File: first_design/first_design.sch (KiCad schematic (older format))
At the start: 56 parts, among them J1 Conn_02x20_Odd_Even, J2 Accelerometer_small, J3 Accelerometer_standard, J4 Servo_motor

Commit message: tracing
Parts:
- removed C7: 44uF, library_express_pro:RLC_EIA_3216, symbol Device:C
- removed D1: 5V, symbol Device:D_Zener
- removed R3: 100K, library_express_pro:RLC_EIA_3216, symbol Device:R
- C2: value 170uF -> 10uF
- SQJA37EP1: footprint (none) -> library_express_pro:SO-8L
- YSL-R531R3D-D1, YSL-R531R3D-D2, YSL-R531R3D-D3, YSL-R531R3D-D4: footprint library_express_pro:LED_YSL-R531R3D-D2 -> library_express_pro:RLC_EIA_3216
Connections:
- wire segments 154 -> 149
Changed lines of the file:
@@
-$EndComp
-$Comp
-L Device:D_Zener D1
-U 1 1 5D2FFD20
-P 1000 1200
-F 0 "D1" V 1046 1121 50  0000 R CNN
-F 1 "5V" V 955 1121 50  0000 R CNN
-F 2 "" H 1000 1200 50  0001 C CNN
-F 3 "~" H 1000 1200 50  0001 C CNN
-	1    1000 1200
-	0    -1   -1   0
 $EndComp
 $Comp
@@
 $EndComp
 Wire Wire Line
-	1000 1000 1500 1000
-Wire Wire Line
-	1000 1050 1000 1000
-Connection ~ 1000 1000
-Wire Wire Line
-	650  1000 1000 1000
-Wire Wire Line
 	1800 1400 1800 1350
 Wire Wire Line
-	1200 1350 1000 1350
-Wire Wire Line
 	1200 1400 1200 1350
-Connection ~ 1200 1350
 Connection ~ 1800 1350
 Wire Wire Line
@@
 P 1200 1550
 F 0 "C2" H 1082 1504 50  0001 R CNN
-F 1 "170uF" H 1082 1550 50  0000 R CNN
+F 1 "10uF" H 1082 1550 50  0000 R CNN
 F 2 "library_express_pro:RLC_EIA_3216" H 1238 1400 50  0001 C CNN
 F 3 "~" H 1200 1550 50  0001 C CNN
@@
 	1    0    0    -1
 $EndComp
-$Comp
-L Device:R R3
-U 1 1 5D63B556
-P 4400 1400
-F 0 "R3" V 4607 1400 50  0000 C CNN
-F 1 "100K" V 4516 1400 50  0000 C CNN
-F 2 "library_express_pro:RLC_EIA_3216" V 4330 1400 50  0001 C CNN
-F 3 "~" H 4400 1400 50  0001 C CNN
-	1    4400 1400
-	-1   0    0    1
-$EndComp
 Text GLabel 4250 1150 0    50   Input ~ 0
 Vbat
@@
 $EndComp
 $Comp
-L Device:C C9
-U 1 1 5D69FBE8
-P 6800 1700
-F 0 "C9" H 6685 1654 50  0000 R CNN
-F 1 "44uF" H 6685 1745 50  0000 R CNN
-F 2 "library_express_pro:RLC_EIA_3216" H 6838 1550 50  0001 C CNN
-F 3 "~" H 6800 1700 50  0001 C CNN
-	1    6800 1700
-	-1   0    0    1
-$EndComp
-$Comp
 L power:GND #PWR0111
 U 1 1 5D6AF0A6
@@
 F 0 "YSL-R531R3D-D2" H 5893 5445 50  0000 C CNN
 F 1 "LED" H 5893 5536 50  0000 C CNN
-F 2 "library_express_pro:LED_YSL-R531R3D-D2" H 5900 5700 50  0001 C CNN
+F 2 "library_express_pro:RLC_EIA_3216" H 5900 5700 50  0001 C CNN
 F 3 "~" H 5900 5700 50  0001 C CNN
 	1    5900 5700
@@
 F 0 "YSL-R531R3D-D1" H 5893 5995 50  0000 C CNN
 F 1 "LED" H 5893 6086 50  0000 C CNN
-F 2 "library_express_pro:LED_YSL-R531R3D-D2" H 5900 6250 50  0001 C CNN
+F 2 "library_express_pro:RLC_EIA_3216" H 5900 6250 50  0001 C CNN
 F 3 "~" H 5900 6250 50  0001 C CNN
 	1    5900 6250
@@
 F 0 "YSL-R531R3D-D3" H 5893 6545 50  0000 C CNN
 F 1 "LED" H 5893 6636 50  0000 C CNN
-F 2 "library_express_pro:LED_YSL-R531R3D-D2" H 5900 6800 50  0001 C CNN
+F 2 "library_express_pro:RLC_EIA_3216" H 5900 6800 50  0001 C CNN
 F 3 "~" H 5900 6800 50  0001 C CNN
 	1    5900 6800
@@
 F 0 "YSL-R531R3D-D4" H 5893 7045 50  0000 C CNN
 F 1 "LED" H 5893 7136 50  0000 C CNN
-F 2 "library_express_pro:LED_YSL-R531R3D-D2" H 5900 7300 50  0001 C CNN
+F 2 "library_express_pro:RLC_EIA_3216" H 5900 7300 50  0001 C CNN
 F 3 "~" H 5900 7300 50  0001 C CNN
 	1    5900 7300
@@
 	4600 1550 4400 1550
 Wire Wire Line
-	4400 1250 4400 1150
-Connection ~ 6800 1550
-Wire Wire Line
-	6800 1550 7000 1550
-Wire Wire Line
-	4600 1150 4400 1150
-Wire Wire Line
-	4250 1150 4400 1150
-Connection ~ 4400 1150
-Wire Wire Line
 	5350 1550 5450 1550
 Wire Wire Line
@@
 Wire Wire Line
 	6100 2300 6100 2650
-$Comp
-L Device:C C7
-U 1 1 5DB9C798
-P 6350 1800
-F 0 "C7" H 6235 1754 50  0000 R CNN
-F 1 "44uF" H 6235 1845 50  0000 R CNN
-F 2 "library_express_pro:RLC_EIA_3216" H 6388 1650 50  0001 C CNN
-F 3 "~" H 6350 1800 50  0001 C CNN
-	1    6350 1800
-	-1   0    0    1
-$EndComp
-Wire Wire Line
-	6350 1650 6100 1650
-Connection ~ 6100 1650
-Wire Wire Line
-	6350 1950 6100 1950
-Wire Wire Line
-	6100 1550 6800 1550
 Connection ~ 6100 1550
 Wire Wire Line
@@
 L Connector_Generic:Conn_01x03 J4
 U 1 1 5DD35231
-P 9800 6050
-F 0 "J4" H 9880 6092 50  0001 L CNN
-F 1 "Servo_motor" H 9880 6046 50  0000 L CNN
-F 2 "library_express_pro:servo_connector" H 9800 6050 50  0001 C CNN
-F 3 "~" H 9800 6050 50  0001 C CNN
-	1    9800 6050
-	1    0    0    -1
-$EndComp
-Text GLabel 9600 5950 0    50   Input ~ 0
+P 9800 6000
+F 0 "J4" H 9880 6042 50  0001 L CNN
+F 1 "Servo_motor" H 9880 5996 50  0000 L CNN
+F 2 "library_express_pro:servo_connector" H 9800 6000 50  0001 C CNN
+F 3 "~" H 9800 6000 50  0001 C CNN
+	1    9800 6000
+	1    0    0    -1
+$EndComp
+Text GLabel 9600 6000 0    50   Input ~ 0
 6V-5V
 $Comp
 L power:GND #PWR0126
 U 1 1 5DD3FB35
-P 9100 6050
-F 0 "#PWR0126" H 9100 5800 50  0001 C CNN
-F 1 "GND" V 9105 5922 50  0000 R CNN
-F 2 "" H 9100 6050 50  0001 C CNN
-F 3 "" H 9100 6050 50  0001 C CNN
-	1    9100 6050
+P 9100 5900
+F 0 "#PWR0126" H 9100 5650 50  0001 C CNN
+F 1 "GND" V 9105 5772 50  0000 R CNN
+F 2 "" H 9100 5900 50  0001 C CNN
+F 3 "" H 9100 5900 50  0001 C CNN
+	1    9100 5900
 	0    1    1    0
 $EndComp
-Text GLabel 9600 6150 0    50   Input ~ 0
+Text GLabel 9600 6100 0    50   Input ~ 0
 servo_PWM
 Wire Wire Line
-	9100 6050 9600 6050
+	9100 5900 9600 5900
 Text GLabel 10000 2900 2    50   Input ~ 0
 servo_PWM
@@
 F 0 "SQJA37EP1" H 1906 1046 50  0000 L CNN
 F 1 "PMOS" H 1906 1000 50  0000 L CNN
-F 2 "" H 1900 1100 50  0001 C CNN
+F 2 "library_express_pro:SO-8L" H 1900 1100 50  0001 C CNN
 F 3 "~" H 1700 1000 50  0001 C CNN
 	1    1700 1000
@@
 	1    0    0    -1
 $EndComp
+Wire Wire Line
+	6100 1550 6800 1550
+Wire Wire Line
+	6800 1550 7000 1550
+Connection ~ 6800 1550
+$Comp
+L Device:C C9
+U 1 1 5D69FBE8
+P 6800 1700
+F 0 "C9" H 6685 1654 50  0000 R CNN
+F 1 "44uF" H 6685 1745 50  0000 R CNN
+F 2 "library_express_pro:RLC_EIA_3216" H 6838 1550 50  0001 C CNN
+F 3 "~" H 6800 1700 50  0001 C CNN
+	1    6800 1700
+	-1   0    0    1
+$EndComp
+Connection ~ 4400 1150
+Wire Wire Line
+	4600 1150 4400 1150
+Wire Wire Line
+	4250 1150 4400 1150
+Wire Wire Line
+	4400 1150 4400 1550
+Wire Wire Line
+	650  1000 1500 1000
 $EndSCHEMATC

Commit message: traced buck
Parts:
- C9: footprint library_express_pro:RLC_EIA_3216 -> library_express_pro:Capacitor_E61
- J1: footprint library_express_pro:RasPi_header_pro -> library_express_pro:RasPi_Header_0.9
- L1: footprint library_express_pro:RLC_EIA_3216 -> library_express_pro:Inductor_PA4340
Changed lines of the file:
@@
 F 0 "J1" V 9654 2013 50  0001 R CNN
 F 1 "Conn_02x20_Odd_Even" H 9745 2013 50  0000 R CNN
-F 2 "library_express_pro:RasPi_header_pro" H 9650 3100 50  0001 C CNN
+F 2 "library_express_pro:RasPi_Header_0.9" H 9650 3100 50  0001 C CNN
 F 3 "~" H 9650 3100 50  0001 C CNN
 	1    9650 3100
@@
 F 0 "L1" V 5519 1550 50  0000 C CNN
 F 1 "3.3uH" V 5610 1550 50  0000 C CNN
-F 2 "library_express_pro:RLC_EIA_3216" H 5700 1550 50  0001 C CNN
+F 2 "library_express_pro:Inductor_PA4340" H 5700 1550 50  0001 C CNN
 F 3 "~" H 5700 1550 50  0001 C CNN
 	1    5700 1550
@@
 F 0 "C9" H 6685 1654 50  0000 R CNN
 F 1 "44uF" H 6685 1745 50  0000 R CNN
-F 2 "library_express_pro:RLC_EIA_3216" H 6838 1550 50  0001 C CNN
+F 2 "library_express_pro:Capacitor_E61" H 6838 1550 50  0001 C CNN
 F 3 "~" H 6800 1700 50  0001 C CNN
 	1    6800 1700

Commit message: Before changes
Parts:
- removed C3: 100nF, library_express_pro:RLC_EIA_3216, symbol Device:C
- removed C8: 10uF, library_express_pro:RLC_EIA_3216, symbol Device:C
- removed R10, R7, R8, R9: 220, library_express_pro:RLC_EIA_3216, symbol Device:R
- removed R11, R12, R13, R14: 82, library_express_pro:RLC_EIA_3216, symbol Device:R
- added U1: Resistor_array, library_express_pro:Resistor_array_YC324, symbol Connector:Resistor_array
- R1: value 220 -> 22.1
- R2: value 220 -> 66.3
- R4, R5: value 10K -> 22.1K
- Rmax1: value 280 -> 22.1K
- renumbered PTS636_G_Leads4 to Button1, PTS636_G_Leads2 to Button2, PTS636_G_Leads1 to Button3, PTS636_G_Leads3 to Button4'1
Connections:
- net labels added: VDC, servo
- net labels removed: +7.5V, 6V-5V
- wire segments 149 -> 147
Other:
- moved on the sheet: Button1, Button2, Button3, LDO1, Power1, R1, R2, YSL-R531R3D-D1, YSL-R531R3D-D2, YSL-R531R3D-D3, YSL-R531R3D-D4

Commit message: working on tracing, back layer is messed up
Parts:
- removed C1: 10uF, library_express_pro:RLC_EIA_3216, symbol Device:C
- removed R5, Rmax1: 22.1K, library_express_pro:RLC_EIA_3216, symbol Device:R
- removed U1: Resistor_array, library_express_pro:Resistor_array_YC324, symbol Connector:Resistor_array
- added IC4: RN, library_express_pro:Resistor_array_YC324, symbol first_design-rescue:RN-Connector
- added JP2, JP3: SolderJumper_3_Bridged12, Jumper:SolderJumper-3_P1.3mm_Open_RoundedPad1.0x1.5mm_NumberLabels, symbol Jumper:SolderJumper_3_Bridged12
- added R3: 66.3k, library_express_pro:RLC_EIA_3216, symbol Device:R
- IC1: renamed from VoltageMonitor1; symbol Sensor_Voltage:BD48K60 -> first_design-rescue:BD48K60-Sensor_Voltage
- IC2: renamed from LDO1; symbol Converter_DCDC:AZ2085 -> first_design-rescue:AZ2085-Converter_DCDC
- IC3: renamed from StepDownConverter1; symbol Converter_DCDC:AP65450 -> first_design-rescue:AP65450-Converter_DCDC
- IC5: renamed from MotorController1; symbol Driver_Motor:VNH7070BAS -> first_design-rescue:VNH7070BAS-Driver_Motor
- R1: value 22.1 -> 22.1k
- R2: value 66.3 -> 66.3k
- YSL-R531R3D-D1: value LED -> LED2
- YSL-R531R3D-D2: value LED -> LED1
- YSL-R531R3D-D3: value LED -> LED3
- YSL-R531R3D-D4: value LED -> LED4
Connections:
- net labels added: GPIO12, GPIO13, GPIO16, GPIO18, GPIO20, GPIO21, GPIO23, GPIO24, GPIO25, GPIO26, GPIO5, GPIO6, VCC, Vservo
- net labels removed: LED1, LED2, LED3, LED4, VDC, button1, button2, button3, button4, motor_INA, motor_INB, motor_PWM, servo, servo_PWM
- wire segments 147 -> 172
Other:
- moved on the sheet: Button1, Button2, Button3, Button4'1, C4, C5, C6, C9, H1, H2, H3, H4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

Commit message: Killing it
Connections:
- net GPIO18: now also IC5.6 (INB); no longer IC5.3 (INA)
- net GPIO23: now also IC5.3 (INA); no longer J4.3 (Pin_3)
- net GPIO24: now also IC5.11 (PWM); no longer IC5.6 (INB)
- net GPIO25: now also J4.3 (Pin_3); no longer IC5.11 (PWM)
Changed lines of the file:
@@
 	8950 1050 9200 1050
 Connection ~ 9200 1050
-Text GLabel 8950 1250 0    50   Input ~ 0
+Text GLabel 8950 1350 0    50   Input ~ 0
 GPIO18
-Text GLabel 8950 1350 0    50   Input ~ 0
+Text GLabel 10250 1150 2    50   Input ~ 0
 GPIO24
 Wire Wire Line
-	8950 1250 9250 1250
+	8950 1350 9250 1350
 Text GLabel 7550 3000 2    50   Input ~ 0
 GPIO18
@@
 	1    0    0    -1
 $EndComp
-Text GLabel 10150 4650 2    50   Input ~ 0
+Text GLabel 8950 1250 0    50   Input ~ 0
 GPIO23
 Wire Wire Line
@@
 	9150 1450 9150 1600
 Wire Wire Line
-	9250 1350 8950 1350
+	9250 1250 8950 1250
 $Comp
 L first_design-rescue:RN-Connector IC4
@@
 Wire Wire Line
 	7000 2500 7000 2400
-Text GLabel 10250 1150 2    50   Input ~ 0
+Text GLabel 10150 4650 2    50   Input ~ 0
 GPIO25
 Text GLabel 7550 3200 2    50   Input ~ 0

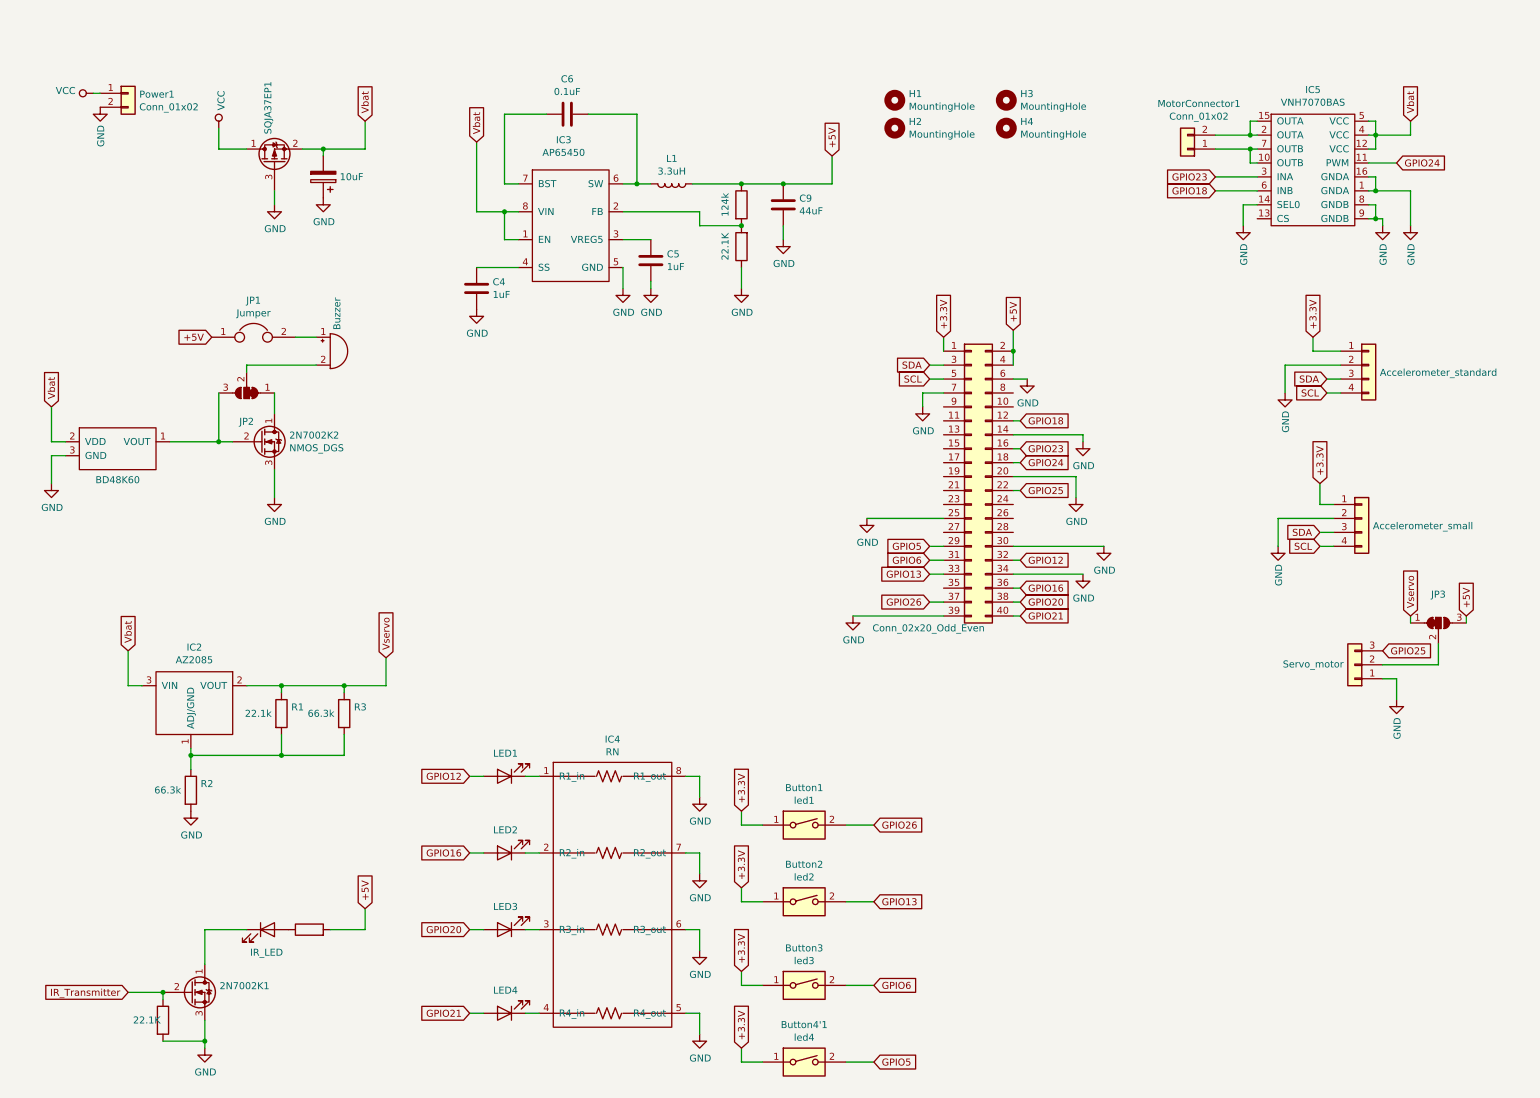
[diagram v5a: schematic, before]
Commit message: Everything is wired, fixed schematic, haven't found PMOS and IR yet. Check PCB design
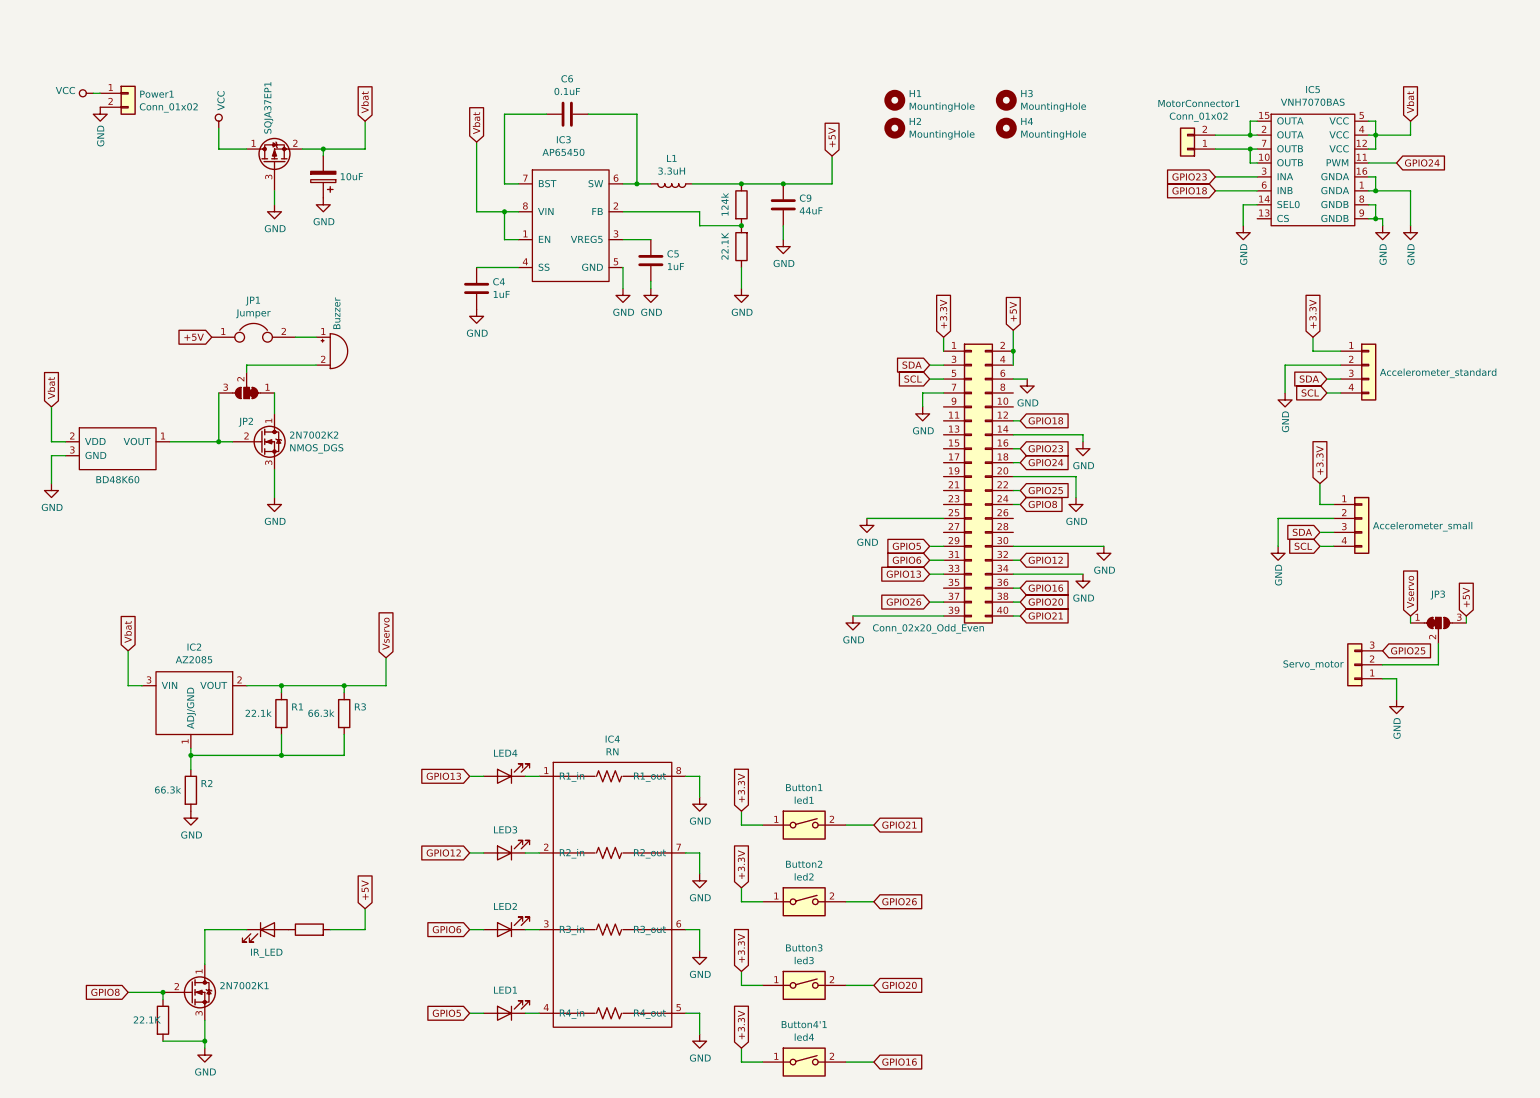
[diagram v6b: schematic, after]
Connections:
- net IR_Transmitter is gone; now on net GPIO8: 2N7002K1.2 (G), R4.1
- net GPIO12: now also YSL-R531R3D-D3.2 (A); no longer YSL-R531R3D-D2.2 (A)
- net GPIO13: now also YSL-R531R3D-D4.2 (A); no longer Button2.2
- net GPIO16: now also Button4'1.2; no longer YSL-R531R3D-D1.2 (A)
- net GPIO20: now also Button3.2; no longer YSL-R531R3D-D3.2 (A)
- net GPIO21: now also Button1.2; no longer YSL-R531R3D-D4.2 (A)
- net GPIO26: now also Button2.2; no longer Button1.2
- net GPIO5: now also YSL-R531R3D-D2.2 (A); no longer Button4'1.2
- net GPIO6: now also YSL-R531R3D-D1.2 (A); no longer Button3.2
- net GPIO8: now reaches J1.24 (Pin_24)
- net at YSL-R531R3D-D2.1 (K): now also IC4.4 (R4_in); no longer IC4.1 (R1_in)
- net at YSL-R531R3D-D1.1 (K): now also IC4.3 (R3_in); no longer IC4.2 (R2_in)
- net at YSL-R531R3D-D3.1 (K): now also IC4.2 (R2_in); no longer IC4.3 (R3_in)
- net at YSL-R531R3D-D4.1 (K): now also IC4.1 (R1_in); no longer IC4.4 (R4_in)
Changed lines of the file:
@@
 $EndComp
 Text GLabel 1150 7100 0    50   Input ~ 0
-IR_Transmitter
+GPIO8
 Text GLabel 2850 6500 1    50   Input ~ 0
 +5V
@@
 Wire Wire Line
 	2250 5250 2250 5400
-Text GLabel 3600 6650 0    50   Input ~ 0
+Text GLabel 6500 7050 2    50   Input ~ 0
 GPIO20
-Text GLabel 3600 7250 0    50   Input ~ 0
+Text GLabel 6500 5900 2    50   Input ~ 0
 GPIO21
 Wire Wire Line
-	3700 7250 3600 7250
+	3700 5550 3600 5550
 $Comp
 L Device:LED YSL-R531R3D-D4
 U 1 1 5D59A2BC
+P 3850 5550
+F 0 "YSL-R531R3D-D4" H 3843 5295 50  0001 C CNN
+F 1 "LED4" H 3843 5386 50  0000 C CNN
+F 2 "library_express_pro:RLC_EIA_3216" H 3850 5550 50  0001 C CNN
+F 3 "~" H 3850 5550 50  0001 C CNN
+	1    3850 5550
+	-1   0    0    1
+$EndComp
+Wire Wire Line
+	3700 6100 3600 6100
+Wire Wire Line
+	3700 7250 3600 7250
+Text GLabel 3600 6100 0    50   Input ~ 0
+GPIO12
+$Comp
+L Device:LED YSL-R531R3D-D2
+U 1 1 5D2A496C
 P 3850 7250
-F 0 "YSL-R531R3D-D4" H 3843 6995 50  0001 C CNN
-F 1 "LED4" H 3843 7086 50  0000 C CNN
+F 0 "YSL-R531R3D-D2" H 3843 6995 50  0001 C CNN
+F 1 "LED1" H 3843 7086 50  0000 C CNN
 F 2 "library_express_pro:RLC_EIA_3216" H 3850 7250 50  0001 C CNN
 F 3 "~" H 3850 7250 50  0001 C CNN
@@
 	-1   0    0    1
 $EndComp
-Wire Wire Line
-	3700 6650 3600 6650
-Wire Wire Line
-	3700 5550 3600 5550
-Text GLabel 3600 5550 0    50   Input ~ 0
-GPIO12
-$Comp
-L Device:LED YSL-R531R3D-D2
-U 1 1 5D2A496C
-P 3850 5550
-F 0 "YSL-R531R3D-D2" H 3843 5295 50  0001 C CNN
-F 1 "LED1" H 3843 5386 50  0000 C CNN
-F 2 "library_express_pro:RLC_EIA_3216" H 3850 5550 50  0001 C CNN
-F 3 "~" H 3850 5550 50  0001 C CNN
-	1    3850 5550
-	-1   0    0    1
-$EndComp
 $Comp
 L Device:LED YSL-R531R3D-D1
 U 1 1 5D5894B2
-P 3850 6100
-F 0 "YSL-R531R3D-D1" H 3843 5845 50  0001 C CNN
-F 1 "LED2" H 3843 5936 50  0000 C CNN
-F 2 "library_express_pro:RLC_EIA_3216" H 3850 6100 50  0001 C CNN
-F 3 "~" H 3850 6100 50  0001 C CNN
-	1    3850 6100
+P 3850 6650
+F 0 "YSL-R531R3D-D1" H 3843 6395 50  0001 C CNN
+F 1 "LED2" H 3843 6486 50  0000 C CNN
+F 2 "library_express_pro:RLC_EIA_3216" H 3850 6650 50  0001 C CNN
+F 3 "~" H 3850 6650 50  0001 C CNN
+	1    3850 6650
 	-1   0    0    1
 $EndComp
 Wire Wire Line
-	3700 6100 3600 6100
-Text GLabel 3600 6100 0    50   Input ~ 0
+	3700 6650 3600 6650
+Text GLabel 6500 7600 2    50   Input ~ 0
 GPIO16
 $Comp
@@
 L Device:LED YSL-R531R3D-D3
 U 1 1 5D591864
-P 3850 6650
-F 0 "YSL-R531R3D-D3" H 3843 6395 50  0001 C CNN
-F 1 "LED3" H 3843 6486 50  0000 C CNN
-F 2 "library_express_pro:RLC_EIA_3216" H 3850 6650 50  0001 C CNN
-F 3 "~" H 3850 6650 50  0001 C CNN
-	1    3850 6650
+P 3850 6100
+F 0 "YSL-R531R3D-D3" H 3843 5845 50  0001 C CNN
+F 1 "LED3" H 3843 5936 50  0000 C CNN
+F 2 "library_express_pro:RLC_EIA_3216" H 3850 6100 50  0001 C CNN
+F 3 "~" H 3850 6100 50  0001 C CNN
+	1    3850 6100
 	-1   0    0    1
 $EndComp
@@
 Wire Wire Line
 	6300 6450 6500 6450
-Text GLabel 6500 7600 2    50   Input ~ 0
+Text GLabel 3600 7250 0    50   Input ~ 0
 GPIO5
-Text GLabel 6500 7050 2    50   Input ~ 0
+Text GLabel 3600 6650 0    50   Input ~ 0
 GPIO6
-Text GLabel 6500 6450 2    50   Input ~ 0
+Text GLabel 3600 5550 0    50   Input ~ 0
 GPIO13
 $Comp
@@
 	1    0    0    -1
 $EndComp
-Text GLabel 6500 5900 2    50   Input ~ 0
+Text GLabel 6500 6450 2    50   Input ~ 0
 GPIO26
 Wire Wire Line
@@
 +3.3V
 Wire Wire Line
+	4100 7250 4000 7250
+Wire Wire Line
+	4100 6650 4000 6650
+Wire Wire Line
+	4100 6100 4000 6100
+Wire Wire Line
 	4100 5550 4000 5550
-Wire Wire Line
-	4100 6100 4000 6100
-Wire Wire Line
-	4100 6650 4000 6650
-Wire Wire Line
-	4100 7250 4000 7250
 Wire Wire Line
 	5150 5550 5250 5550
@@
 Wire Wire Line
 	2000 2600 2500 2600
+Text GLabel 7550 3600 2    50   Input ~ 0
+GPIO8
+Wire Wire Line
+	7500 3600 7550 3600
 $EndSCHEMATC
